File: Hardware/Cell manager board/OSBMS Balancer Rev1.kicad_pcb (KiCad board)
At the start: 2 copper layers, 49 x 50.7 mm, 74 parts, among them P1 CONN_01X07, P2 EXT-TMP, P3 CONN_01X09, P4 CONN_01X09, P5 CONN_01X01, Q1 BSS138, Q2 BSS138, Q3 BSS138, Q4 BSS138, Q5 BSS138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

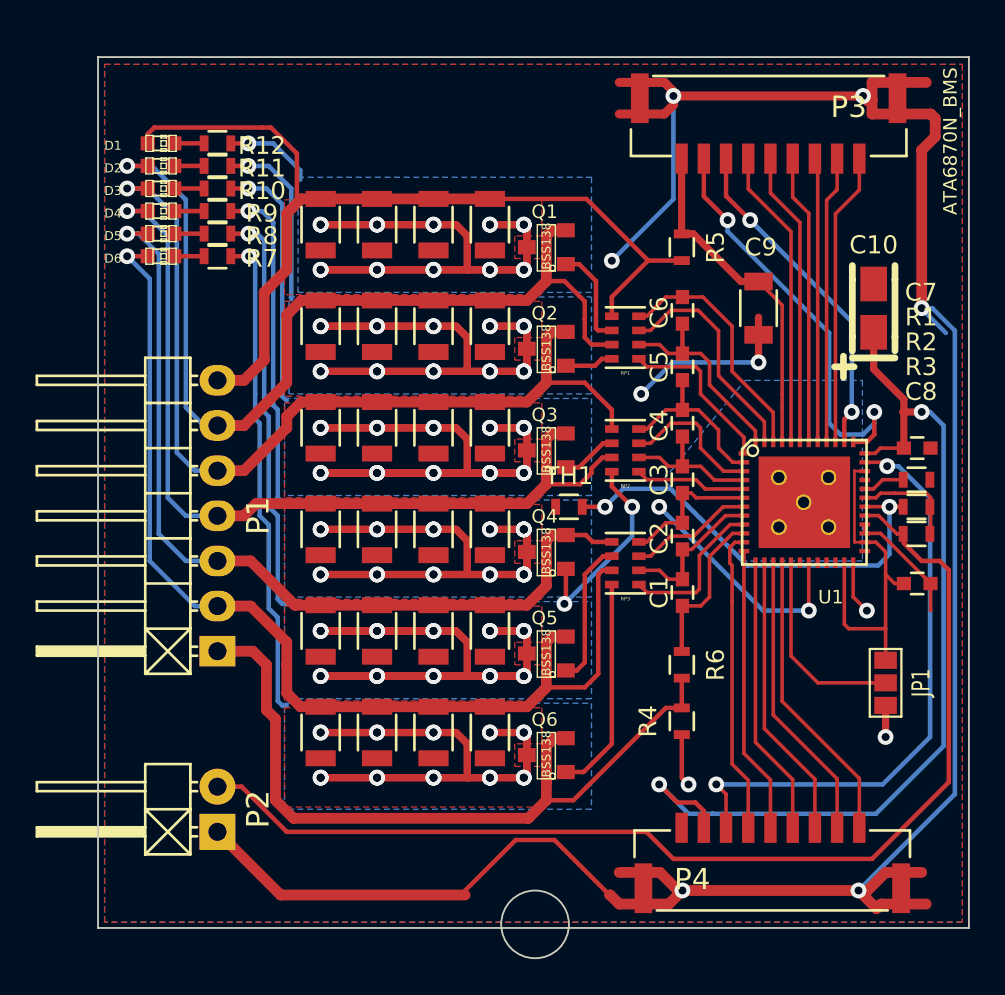
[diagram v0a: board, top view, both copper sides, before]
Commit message: touched up balancer board and reorganised
touched up balancer board so that it is ready for production,
reorganised a bunch of files and added proper revision labels, and made
good progress on the micromaster board. the schematic is complete, the
board is layed out, some traces still need to be run though.
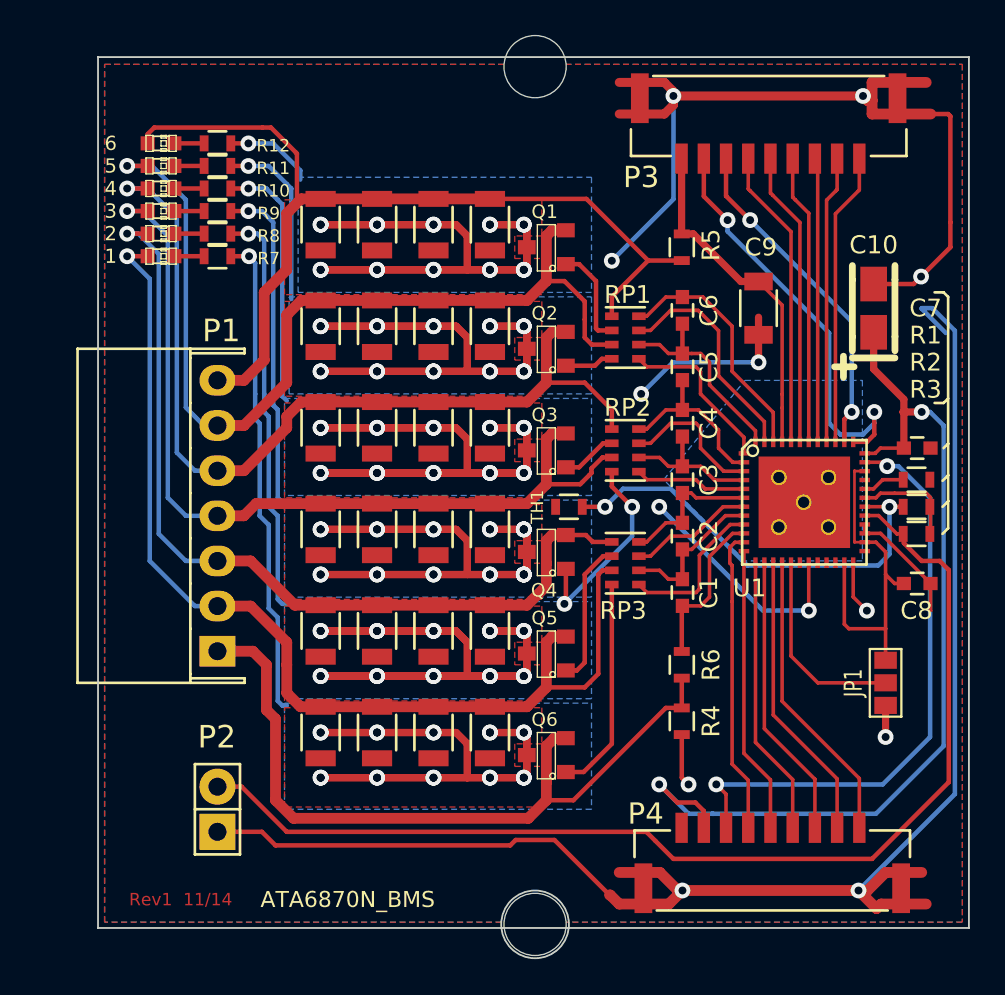
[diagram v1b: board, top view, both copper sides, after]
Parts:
- added MH: MountingHole_3-5mm_RevA_Date21Jun2010, Mounting_Holes:MountingHole_3-5mm, F.Cu at (190.6, 105.5)
- added MH: MountingHole_3-5mm_RevA_Date21Jun2010, Mounting_Holes:MountingHole_3-5mm, F.Cu at (190.6, 153.8)
- P1: footprint Pin_Headers:Pin_Header_Angled_1x07 -> MyCustomParts:Shrouded_Header_Angled_1x07
- P2: footprint Pin_Headers:Pin_Header_Angled_1x02 -> Pin_Headers:Pin_Header_Straight_1x02
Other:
- board text added: "1"
- board text added: "2"
- board text added: "3"
- board text added: "4"
- board text added: "5"
- board text added: "6"
- board text added: "Rev1 11/14"
